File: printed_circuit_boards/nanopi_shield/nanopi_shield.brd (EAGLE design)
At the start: 48.2 x 42.9 mm, 4 parts, among them X1 1365-40

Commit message: Round corner
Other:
- outline, holes or cut-outs redrawn
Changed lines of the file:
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@@
 <board>
 <plain>
-<wire x1="0" y1="0" x2="16.51" y2="0" width="0" layer="20"/>
-<wire x1="16.51" y1="0" x2="16.464871875" y2="23.449871875" width="0" layer="20"/>
+<wire x1="0" y1="42.85" x2="0" y2="5.08" width="0" layer="20"/>
+<wire x1="0" y1="5.08" x2="5.08" y2="0" width="0" layer="20"/>
+<wire x1="5.08" y1="0" x2="9.529884375" y2="0" width="0" layer="20"/>
+<wire x1="9.529884375" y1="0" x2="16.496565625" y2="6.9808875" width="0" layer="20"/>
+<wire x1="16.496565625" y1="6.9808875" x2="16.464871875" y2="23.449871875" width="0" layer="20"/>
 <wire x1="16.464871875" y1="23.449871875" x2="48.24" y2="23.449871875" width="0" layer="20"/>
 <wire x1="48.24" y1="23.449871875" x2="48.24" y2="42.85" width="0" layer="20"/>
 <wire x1="48.24" y1="42.85" x2="0" y2="42.85" width="0" layer="20"/>
-<wire x1="0" y1="42.85" x2="0" y2="0" width="0" layer="20"/>
 </plain>
 <attributes>
@@
 <contactref element="X1" pad="13"/>
 <contactref element="X1" pad="19"/>
-<polygon width="0.8128" layer="16" isolate="0.508" thermals="no">
-<vertex x="16.51" y="0"/>
-<vertex x="0" y="0"/>
+<polygon width="0.1524" layer="16" isolate="0.4572" thermals="no">
+<vertex x="35.56" y="42.545"/>
+<vertex x="35.56" y="36.83"/>
+<vertex x="6.35" y="36.83"/>
+<vertex x="6.35" y="8.255"/>
+<vertex x="12.065" y="2.54"/>
+<vertex x="9.525" y="0"/>
+<vertex x="5.08" y="0"/>
+<vertex x="0" y="5.08"/>
 <vertex x="0" y="42.545"/>
-<vertex x="48.26" y="42.545"/>
-<vertex x="48.26" y="23.495"/>
-<vertex x="16.51" y="23.495"/>
 </polygon>
-<wire x1="29.845" y1="37.24" x2="33.655" y2="37.24" width="0" layer="19" extent="16-16"/>
-<wire x1="24.765" y1="37.24" x2="29.845" y2="37.24" width="0" layer="19" extent="16-16"/>
-<wire x1="3.175" y1="36.83" x2="24.765" y2="37.24" width="0" layer="19" extent="16-16"/>
 </signal>
 <signal name="I2C3_SCL">

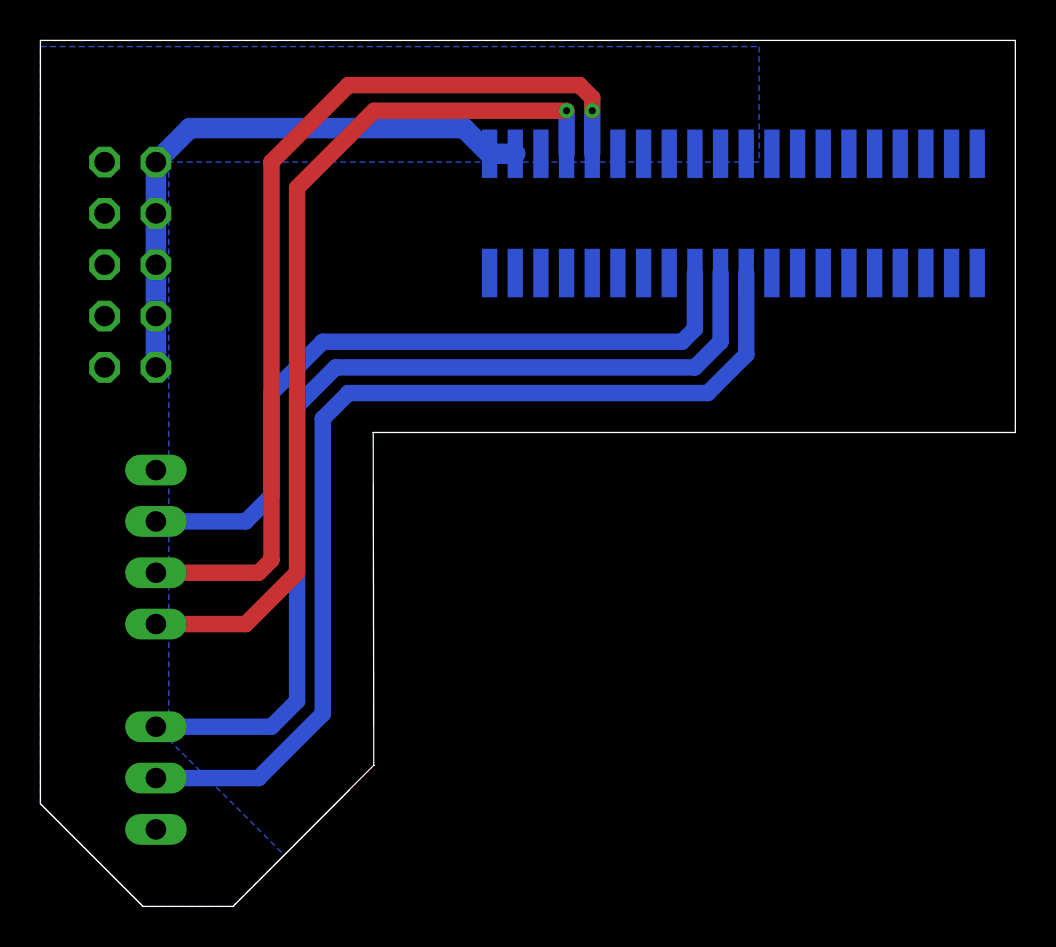
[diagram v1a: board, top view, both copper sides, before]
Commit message: Larger pads
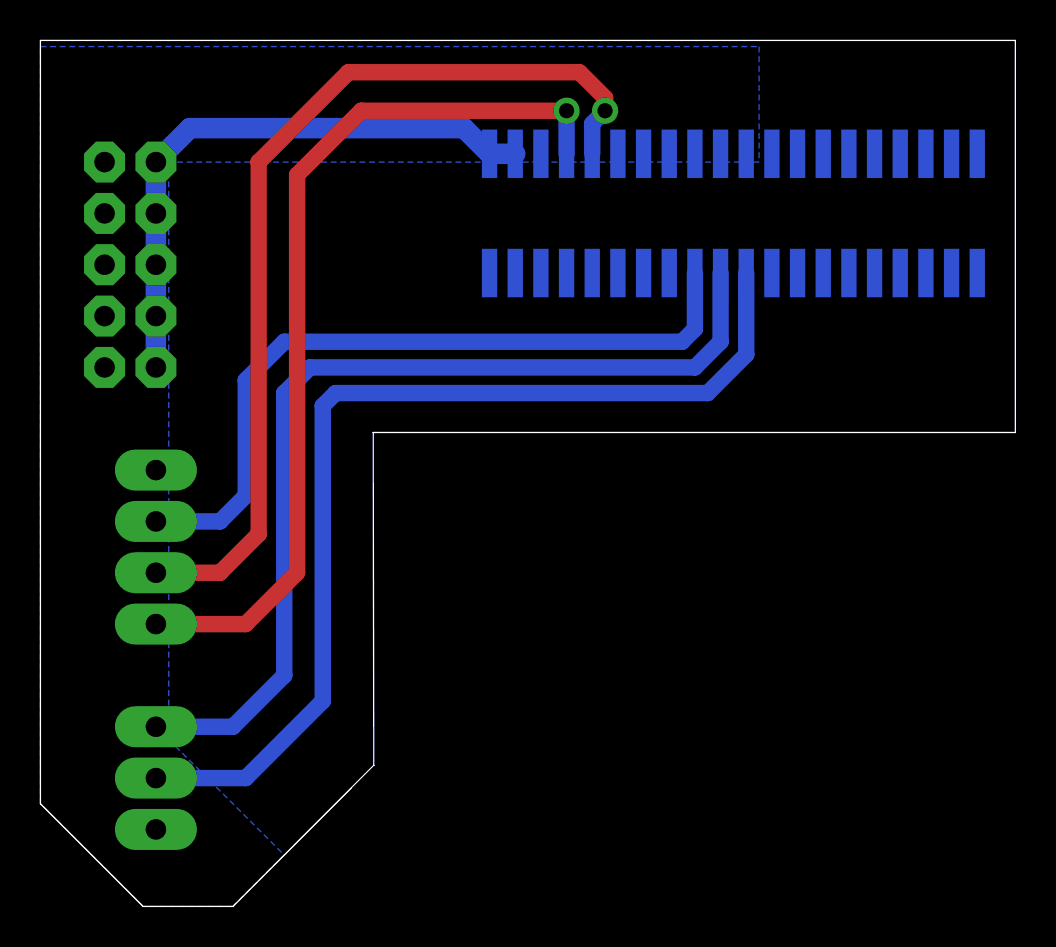
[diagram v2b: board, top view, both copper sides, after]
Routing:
- net I2C3_SDA: track 46.1 -> 46.8 mm
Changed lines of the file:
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@@
 <drawing>
 <settings>
-<setting alwaysvectorfont="no"/>
+<setting alwaysvectorfont="yes"/>
 <setting verticaltext="up"/>
 </settings>
@@
 </class>
 </classes>
-<designrules name="default">
+<designrules name="default *">
 <description language="de">&lt;b&gt;EAGLE Design Rules&lt;/b&gt;
 &lt;p&gt;
@@
 <param name="mnLayersViaInSmd" value="2"/>
 <param name="mdCopperDimension" value="40mil"/>
-<param name="mdDrill" value="6mil"/>
+<param name="mdDrill" value="12mil"/>
 <param name="mdSmdStop" value="0mil"/>
-<param name="msWidth" value="6mil"/>
+<param name="msWidth" value="12mil"/>
 <param name="msDrill" value="0.35mm"/>
 <param name="msMicroVia" value="9.99mm"/>
@@
 <param name="rvMicroViaOuter" value="0.25"/>
 <param name="rvMicroViaInner" value="0.25"/>
-<param name="rlMinPadTop" value="10mil"/>
+<param name="rlMinPadTop" value="20mil"/>
 <param name="rlMaxPadTop" value="20mil"/>
-<param name="rlMinPadInner" value="10mil"/>
+<param name="rlMinPadInner" value="20mil"/>
 <param name="rlMaxPadInner" value="20mil"/>
-<param name="rlMinPadBottom" value="10mil"/>
+<param name="rlMinPadBottom" value="20mil"/>
 <param name="rlMaxPadBottom" value="20mil"/>
 <param name="rlMinViaOuter" value="8mil"/>
@@
 <attribute name="NAME" x="7.5438" y="2.4638" size="1.27" layer="26" ratio="10" rot="MR90"/>
 <attribute name="POPULARITY" value="92" x="-18.415" y="35.56" size="1.778" layer="28" rot="MR90" display="off"/>
-<attribute name="VALUE" x="2.54" y="2.54" size="1.27" layer="28" rot="MR90"/>
 </element>
 <element name="JP2" library="pinhead" library_urn="urn:adsk.eagle:library:325" package="1X04" package3d_urn="urn:adsk.eagle:package:22407/2" value="I2C" x="5.715" y="17.78" smashed="yes" rot="MR270">
 <attribute name="NAME" x="3.8862" y="22.9362" size="1.27" layer="26" ratio="10" rot="MR270"/>
 <attribute name="POPULARITY" value="91" x="29.845" y="-1.27" size="1.778" layer="28" rot="MR270" display="off"/>
-<attribute name="VALUE" x="12.065" y="22.86" size="1.27" layer="28" rot="MR270"/>
 </element>
 <element name="JP3" library="pinhead" library_urn="urn:adsk.eagle:library:325" package="2X05" package3d_urn="urn:adsk.eagle:package:22470/2" value="PWR" x="4.445" y="31.75" smashed="yes" rot="MR90">
 <attribute name="NAME" x="7.62" y="25.4" size="1.27" layer="26" ratio="10" rot="MR90"/>
 <attribute name="POPULARITY" value="35" x="-0.635" y="52.07" size="1.778" layer="28" rot="MR90" display="off"/>
-<attribute name="VALUE" x="0" y="25.4" size="1.27" layer="28" rot="MR90"/>
 </element>
 <element name="X1" library="con-leotronics" library_urn="urn:adsk.eagle:library:160" package="1365-40" package3d_urn="urn:adsk.eagle:package:7973/1" value="1365-40" x="34.29" y="34.29" smashed="yes" rot="MR180">
@@
 <attribute name="OC_NEWARK" value="unknown" x="62.23" y="49.53" size="1.778" layer="28" rot="MR180" display="off"/>
 <attribute name="POPULARITY" value="0" x="62.23" y="49.53" size="1.778" layer="28" rot="MR180" display="off"/>
-<attribute name="VALUE" x="48.895" y="38.1" size="1.27" layer="28" rot="MR270"/>
 </element>
 </elements>
@@
 <contactref element="X1" pad="7"/>
 <wire x1="10.16" y1="13.97" x2="12.7" y2="16.51" width="0.8128" layer="1"/>
-<wire x1="12.7" y1="35.56" x2="16.51" y2="39.37" width="0.8128" layer="1"/>
-<wire x1="16.51" y1="39.37" x2="26.035" y2="39.37" width="0.8128" layer="1"/>
-<wire x1="12.7" y1="16.51" x2="12.7" y2="35.56" width="0.8128" layer="1"/>
-<via x="26.035" y="39.37" extent="1-16" drill="0.35"/>
+<wire x1="12.7" y1="36.195" x2="15.875" y2="39.37" width="0.8128" layer="1"/>
+<wire x1="15.875" y1="39.37" x2="26.035" y2="39.37" width="0.8128" layer="1"/>
+<wire x1="12.7" y1="16.51" x2="12.7" y2="36.195" width="0.8128" layer="1"/>
+<via x="26.035" y="39.37" extent="1-16" drill="0.75" diameter="1.3"/>
 <wire x1="26.035" y1="39.37" x2="26.035" y2="37.24" width="0.8128" layer="16"/>
 <wire x1="10.16" y1="13.97" x2="5.715" y2="13.97" width="0.8128" layer="1"/>
@@
 <contactref element="JP2" pad="3"/>
 <contactref element="X1" pad="9"/>
-<wire x1="11.43" y1="36.83" x2="11.43" y2="17.145" width="0.8128" layer="1"/>
-<wire x1="11.43" y1="17.145" x2="10.795" y2="16.51" width="0.8128" layer="1"/>
-<wire x1="11.43" y1="36.83" x2="15.24" y2="40.64" width="0.8128" layer="1"/>
-<wire x1="26.67" y1="40.64" x2="27.305" y2="40.005" width="0.8128" layer="1"/>
-<wire x1="27.305" y1="40.005" x2="27.305" y2="39.37" width="0.8128" layer="1"/>
-<wire x1="15.24" y1="40.64" x2="26.67" y2="40.64" width="0.8128" layer="1"/>
-<via x="27.305" y="39.37" extent="1-16" drill="0.35"/>
-<wire x1="27.305" y1="39.37" x2="27.305" y2="37.24" width="0.8128" layer="16"/>
-<wire x1="10.795" y1="16.51" x2="5.715" y2="16.51" width="0.8128" layer="1"/>
+<wire x1="10.795" y1="36.83" x2="10.795" y2="18.415" width="0.8128" layer="1"/>
+<wire x1="10.795" y1="18.415" x2="8.89" y2="16.51" width="0.8128" layer="1"/>
+<wire x1="10.795" y1="36.83" x2="15.24" y2="41.275" width="0.8128" layer="1"/>
+<wire x1="26.67" y1="41.275" x2="15.24" y2="41.275" width="0.8128" layer="1"/>
+<wire x1="27.94" y1="40.005" x2="26.67" y2="41.275" width="0.8128" layer="1"/>
+<wire x1="27.94" y1="40.005" x2="27.94" y2="39.37" width="0.8128" layer="1"/>
+<via x="27.94" y="39.37" extent="1-16" drill="0.75" diameter="1.3"/>
+<wire x1="27.94" y1="39.37" x2="27.305" y2="38.735" width="0.8128" layer="16"/>
+<wire x1="27.305" y1="38.735" x2="27.305" y2="37.24" width="0.8128" layer="16"/>
+<wire x1="8.89" y1="16.51" x2="5.715" y2="16.51" width="0.8128" layer="1"/>
 </signal>
 <signal name="N$23">
@@
 <wire x1="32.385" y1="31.34" x2="32.385" y2="28.575" width="0.8128" layer="16"/>
 <wire x1="32.385" y1="28.575" x2="31.75" y2="27.94" width="0.8128" layer="16"/>
-<wire x1="31.75" y1="27.94" x2="13.97" y2="27.94" width="0.8128" layer="16"/>
-<wire x1="13.97" y1="27.94" x2="11.43" y2="25.4" width="0.8128" layer="16"/>
-<wire x1="11.43" y1="25.4" x2="11.43" y2="20.32" width="0.8128" layer="16"/>
-<wire x1="11.43" y1="20.32" x2="10.16" y2="19.05" width="0.8128" layer="16"/>
-<wire x1="10.16" y1="19.05" x2="5.715" y2="19.05" width="0.8128" layer="16"/>
+<wire x1="31.75" y1="27.94" x2="12.065" y2="27.94" width="0.8128" layer="16"/>
+<wire x1="12.065" y1="27.94" x2="10.16" y2="26.035" width="0.8128" layer="16"/>
+<wire x1="10.16" y1="26.035" x2="10.16" y2="20.32" width="0.8128" layer="16"/>
+<wire x1="10.16" y1="20.32" x2="8.89" y2="19.05" width="0.8128" layer="16"/>
+<wire x1="8.89" y1="19.05" x2="5.715" y2="19.05" width="0.8128" layer="16"/>
 </signal>
 <signal name="UART_TX">
@@
 <wire x1="33.655" y1="31.34" x2="33.655" y2="27.94" width="0.8128" layer="16"/>
 <wire x1="33.655" y1="27.94" x2="32.385" y2="26.67" width="0.8128" layer="16"/>
-<wire x1="32.385" y1="26.67" x2="14.605" y2="26.67" width="0.8128" layer="16"/>
-<wire x1="14.605" y1="26.67" x2="12.7" y2="24.765" width="0.8128" layer="16"/>
-<wire x1="12.7" y1="24.765" x2="12.7" y2="10.16" width="0.8128" layer="16"/>
-<wire x1="12.7" y1="10.16" x2="11.43" y2="8.89" width="0.8128" layer="16"/>
-<wire x1="11.43" y1="8.89" x2="5.715" y2="8.89" width="0.8128" layer="16"/>
+<wire x1="32.385" y1="26.67" x2="13.335" y2="26.67" width="0.8128" layer="16"/>
+<wire x1="13.335" y1="26.67" x2="12.065" y2="25.4" width="0.8128" layer="16"/>
+<wire x1="12.065" y1="25.4" x2="12.065" y2="11.43" width="0.8128" layer="16"/>
+<wire x1="12.065" y1="11.43" x2="9.525" y2="8.89" width="0.8128" layer="16"/>
+<wire x1="9.525" y1="8.89" x2="5.715" y2="8.89" width="0.8128" layer="16"/>
 </signal>
 <signal name="UART_RX">
 <contactref element="JP1" pad="2"/>
 <contactref element="X1" pad="22"/>
-<wire x1="5.715" y1="6.35" x2="10.795" y2="6.35" width="0.8128" layer="16"/>
-<wire x1="10.795" y1="6.35" x2="13.97" y2="9.525" width="0.8128" layer="16"/>
-<wire x1="13.97" y1="9.525" x2="13.97" y2="24.13" width="0.8128" layer="16"/>
-<wire x1="13.97" y1="24.13" x2="15.24" y2="25.4" width="0.8128" layer="16"/>
+<wire x1="5.715" y1="6.35" x2="10.16" y2="6.35" width="0.8128" layer="16"/>
+<wire x1="10.16" y1="6.35" x2="13.97" y2="10.16" width="0.8128" layer="16"/>
+<wire x1="13.97" y1="10.16" x2="13.97" y2="24.765" width="0.8128" layer="16"/>
+<wire x1="13.97" y1="24.765" x2="14.605" y2="25.4" width="0.8128" layer="16"/>
 <wire x1="33.02" y1="25.4" x2="34.925" y2="27.305" width="0.8128" layer="16"/>
 <wire x1="34.925" y1="27.305" x2="34.925" y2="31.34" width="0.8128" layer="16"/>
-<wire x1="15.24" y1="25.4" x2="33.02" y2="25.4" width="0.8128" layer="16"/>
+<wire x1="14.605" y1="25.4" x2="33.02" y2="25.4" width="0.8128" layer="16"/>
 </signal>
 <signal name="N$50">
